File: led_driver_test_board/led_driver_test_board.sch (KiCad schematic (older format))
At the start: 112 parts, among them P1 CONN_01X06_M50-3530642, P2 CONN_01X06_M50-3530642, P3 CONN_01X06_M50-3530642, P4 CONN_01X06_M50-3530642, P5 CONN_01X06_M50-3530642, Q1 Q_NMOS_SSM3K09FULF, Q2 Q_NMOS_SSM3K09FULF, Q3 Q_NMOS_SSM3K09FULF, Q4 Q_NMOS_SSM3K09FULF, Q5 Q_NMOS_SSM3K09FULF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

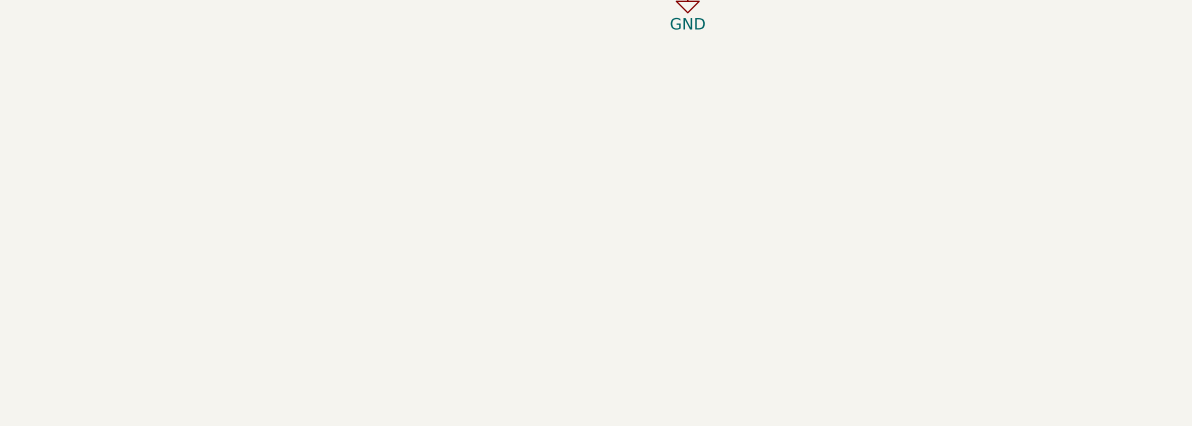
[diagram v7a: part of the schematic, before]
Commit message: Updated title block to current revision 1.1
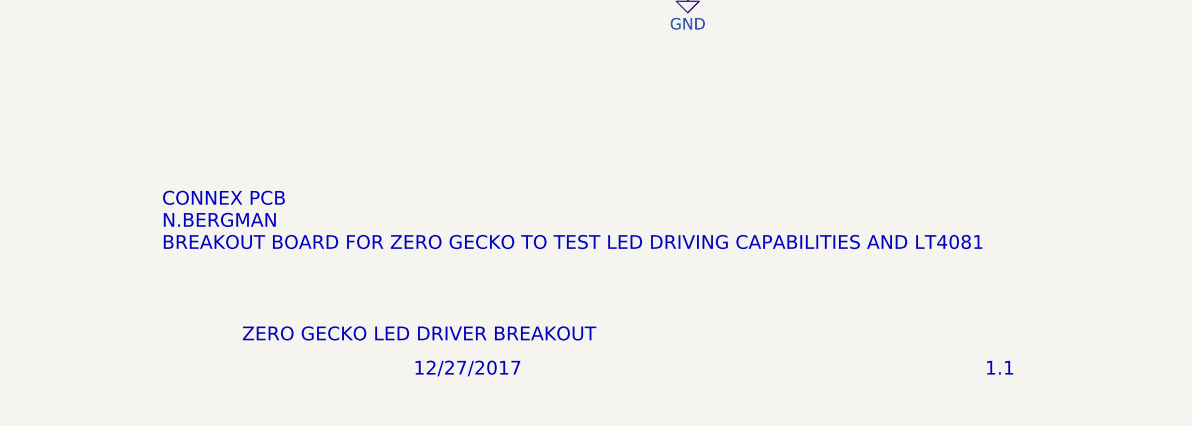
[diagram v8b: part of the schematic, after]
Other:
- note added: "1.1"
- note added: "12/27/2017"
- note added: "CONNEX PCB\nN.BERGMAN\nBREAKOUT BOARD FOR ZERO GECKO TO TEST LED DRIVING CAPABILITIES AND LT4081"
- note added: "ZERO GECKO LED DRIVER BREAKOUT"
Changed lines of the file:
@@
 $EndComp
 NoConn ~ 6700 4650
+Text Notes 7350 7500 0    60   ~ 0
+ZERO GECKO LED DRIVER BREAKOUT
+Text Notes 10600 7650 0    60   ~ 0
+1.1
+Text Notes 8100 7650 0    60   ~ 0
+12/27/2017
+Text Notes 7000 7100 0    60   ~ 0
+CONNEX PCB\nN.BERGMAN\nBREAKOUT BOARD FOR ZERO GECKO TO TEST LED DRIVING CAPABILITIES AND LT4081
 $EndSCHEMATC
